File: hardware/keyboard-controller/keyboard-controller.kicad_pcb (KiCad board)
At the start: 2 copper layers, 34 parts, among them J1 Keybed_Connector, J2 Barrel_Jack_Switch, J3 Debug_Pins, J4 CV_OUT, J5 GATE_OUT, U1 L78L09_TO92, U2 LM358, U3 74HC164, U4 74HC164, U5 TL431LP, U6 LM1117-3.3, U7 Pico, U8 MCP4921

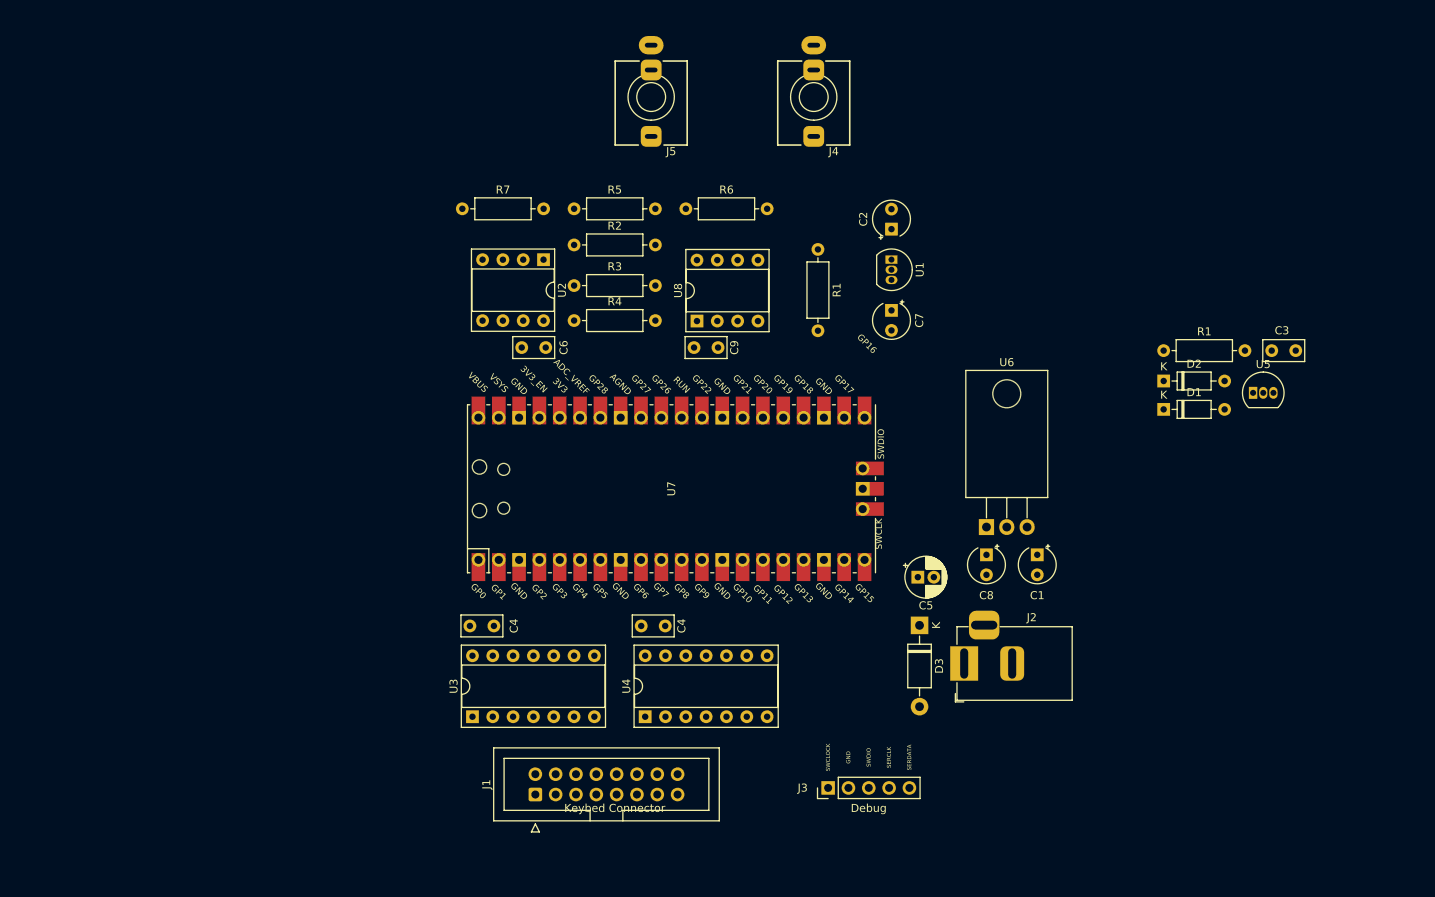
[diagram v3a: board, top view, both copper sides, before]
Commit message: Updated hardware_config and fixed sync_cn
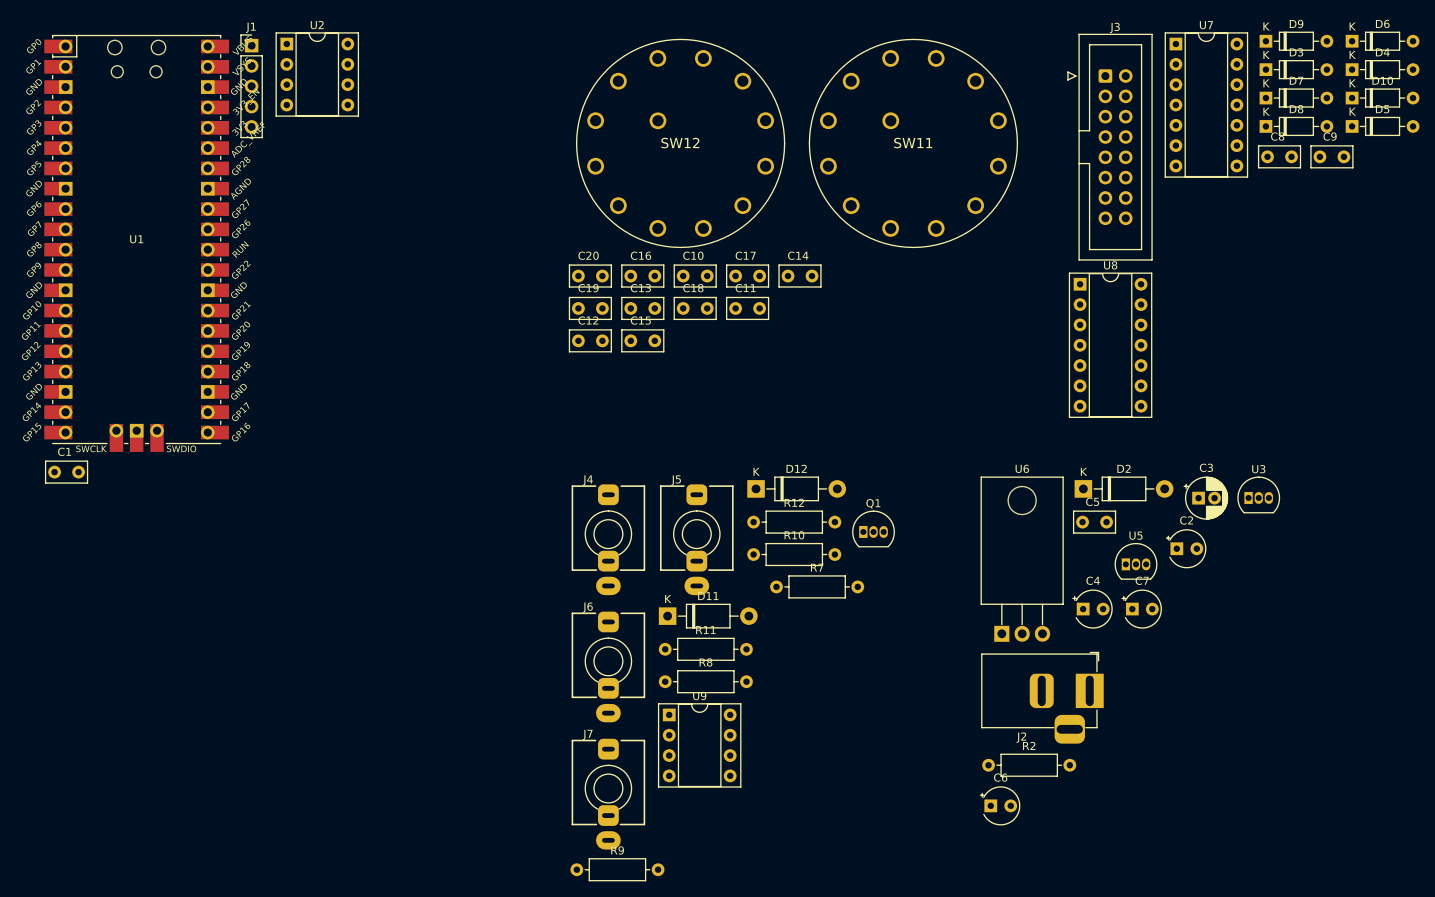
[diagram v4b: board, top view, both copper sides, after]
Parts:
- removed the C4 at (109.9, 114.3)
- removed the C4 at (128.3, 114.3)
- removed D1: 1N4148, Diode_THT:D_DO-35_SOD27_P7.62mm_Horizontal
- removed R1 (x2): 100, Royal_Ohm_Resistors:R_Axial_DIN0207_L6.8mm_D2.5mm_P10.16mm_Horizontal
- removed R3, R4: 10K, Royal_Ohm_Resistors:R_Axial_DIN0207_L6.8mm_D2.5mm_P10.16mm_Horizontal
- removed R5: 22K, Royal_Ohm_Resistors:R_Axial_DIN0207_L6.8mm_D2.5mm_P10.16mm_Horizontal
- removed R6: 1K, Royal_Ohm_Resistors:R_Axial_DIN0207_L6.8mm_D2.5mm_P10.16mm_Horizontal
- removed U4: 74HC164, Package_DIP:DIP-14_W7.62mm_Socket
- added C10: 0.1uF, AEC_Capacitors:C_Disc_D5.0mm_W2.5mm_P3.0mm, F.Cu at (133.6, 70.6)
- added C11: 0.1uF, AEC_Capacitors:C_Disc_D5.0mm_W2.5mm_P3.0mm, F.Cu at (140.1, 74.6)
- added C12: 0.1uF, AEC_Capacitors:C_Disc_D5.0mm_W2.5mm_P3.0mm, F.Cu at (120.5, 78.7)
- added C13: 0.1uF, AEC_Capacitors:C_Disc_D5.0mm_W2.5mm_P3.0mm, F.Cu at (127.0, 74.6)
- added C14: 0.1uF, AEC_Capacitors:C_Disc_D5.0mm_W2.5mm_P3.0mm, F.Cu at (146.7, 70.6)
- added C15: 0.1uF, AEC_Capacitors:C_Disc_D5.0mm_W2.5mm_P3.0mm, F.Cu at (127.0, 78.7)
- added C16: 0.1uF, AEC_Capacitors:C_Disc_D5.0mm_W2.5mm_P3.0mm, F.Cu at (127.0, 70.6)
- added C17: 0.1uF, AEC_Capacitors:C_Disc_D5.0mm_W2.5mm_P3.0mm, F.Cu at (140.1, 70.6)
- added C18: 0.1uF, AEC_Capacitors:C_Disc_D5.0mm_W2.5mm_P3.0mm, F.Cu at (133.6, 74.6)
- added C19: 0.1uF, AEC_Capacitors:C_Disc_D5.0mm_W2.5mm_P3.0mm, F.Cu at (120.5, 74.6)
- added C20: 0.1uF, AEC_Capacitors:C_Disc_D5.0mm_W2.5mm_P3.0mm, F.Cu at (120.5, 70.6)
- added C4: 0.1uF, Capacitor_THT:CP_Radial_Tantal_D4.5mm_P2.50mm, F.Cu at (183.5, 112.2)
- added D10: 1N4148, Diode_THT:D_DO-35_SOD27_P7.62mm_Horizontal, F.Cu at (217.2, 48.3)
- added D11: 1N5818, Diode_THT:D_DO-41_SOD81_P10.16mm_Horizontal, F.Cu at (131.6, 113.1)
- added D12: 1N5818, Diode_THT:D_DO-41_SOD81_P10.16mm_Horizontal, F.Cu at (142.6, 97.2)
- added D4: 1N4148, Diode_THT:D_DO-35_SOD27_P7.62mm_Horizontal, F.Cu at (217.2, 44.8)
- added D5: 1N4148, Diode_THT:D_DO-35_SOD27_P7.62mm_Horizontal, F.Cu at (217.2, 51.9)
- added D6: 1N4148, Diode_THT:D_DO-35_SOD27_P7.62mm_Horizontal, F.Cu at (217.2, 41.2)
- added D7: 1N4148, Diode_THT:D_DO-35_SOD27_P7.62mm_Horizontal, F.Cu at (206.4, 48.3)
- added D8: 1N4148, Diode_THT:D_DO-35_SOD27_P7.62mm_Horizontal, F.Cu at (206.4, 51.9)
- added D9: 1N4148, Diode_THT:D_DO-35_SOD27_P7.62mm_Horizontal, F.Cu at (206.4, 41.2)
- added J6: GATE_OUT, AudioJacks:Jack_3.5mm_QingPu_WQP-PJ398SM_Vertical, F.Cu at (124.2, 118.7)
- added J7: SYNC_OUT, AudioJacks:Jack_3.5mm_QingPu_WQP-PJ398SM_Vertical, F.Cu at (124.2, 134.6)
- added Q1: 2N3904, Package_TO_SOT_THT:TO-92_Inline, F.Cu at (156.1, 102.6)
- added R10: 22K, Royal_Ohm_Resistors:R_Axial_DIN0207_L6.8mm_D2.5mm_P10.16mm_Horizontal, F.Cu at (142.3, 105.4)
- added R11: 1K, Royal_Ohm_Resistors:R_Axial_DIN0207_L6.8mm_D2.5mm_P10.16mm_Horizontal, F.Cu at (131.3, 117.2)
- added R12: 1K, Royal_Ohm_Resistors:R_Axial_DIN0207_L6.8mm_D2.5mm_P10.16mm_Horizontal, F.Cu at (142.3, 101.3)
- added R8: 10K, Royal_Ohm_Resistors:R_Axial_DIN0207_L6.8mm_D2.5mm_P10.16mm_Horizontal, F.Cu at (131.3, 121.3)
- added R9: 10K, Royal_Ohm_Resistors:R_Axial_DIN0207_L6.8mm_D2.5mm_P10.16mm_Horizontal, F.Cu at (120.2, 144.8)
- added SW11: CLK_DIV, SamacSys_Parts:SR2612F011221R0BD8N, F.Cu at (151.7, 51.1)
- added SW12: SUB_MODE, SamacSys_Parts:SR2612F011221R0BD8N, F.Cu at (122.6, 51.1)
- added U9: LM358, Package_DIP:DIP-8_W7.62mm_Socket, F.Cu at (131.8, 125.4)
- C1: value 0.33uF -> 0.1uF; footprint Capacitor_THT:CP_Radial_Tantal_D4.5mm_P2.50mm -> AEC_Capacitors:C_Disc_D5.0mm_W2.5mm_P3.0mm
- C2: value 0.1uF -> 0.33uF
- C3: value 0.1uF -> 47uF; footprint AEC_Capacitors:C_Disc_D5.0mm_W2.5mm_P3.0mm -> Capacitor_THT:CP_Radial_D5.0mm_P2.00mm
- C5: value 47uF -> 0.1uF; footprint Capacitor_THT:CP_Radial_D5.0mm_P2.00mm -> AEC_Capacitors:C_Disc_D5.0mm_W2.5mm_P3.0mm
- C6: value 0.1uF -> 10uF; footprint AEC_Capacitors:C_Disc_D5.0mm_W2.5mm_P3.0mm -> Capacitor_THT:CP_Radial_Tantal_D4.5mm_P2.50mm
- C8: value 100uF -> 0.1uF; footprint Capacitor_THT:CP_Radial_Tantal_D4.5mm_P2.50mm -> AEC_Capacitors:C_Disc_D5.0mm_W2.5mm_P3.0mm
- D2: value 1N4148 -> 1N4001; footprint Diode_THT:D_DO-35_SOD27_P7.62mm_Horizontal -> Diode_THT:D_DO-41_SOD81_P10.16mm_Horizontal
- D3: value 1N5818 -> 1N4148; footprint Diode_THT:D_DO-41_SOD81_P10.16mm_Horizontal -> Diode_THT:D_DO-35_SOD27_P7.62mm_Horizontal
- J1: value Keybed_Connector -> Debug_Pins; footprint Connector_IDC:IDC-Header_2x08_P2.54mm_Vertical -> Connector_PinHeader_2.54mm:PinHeader_1x05_P2.54mm_Vertical
- J3: value Debug_Pins -> Keybed_Connector; footprint Connector_PinHeader_2.54mm:PinHeader_1x05_P2.54mm_Vertical -> Connector_IDC:IDC-Header_2x08_P2.54mm_Vertical
- J4: value CV_OUT -> SYNC_IN
- J5: value GATE_OUT -> CV_OUT
- R2: value 10K -> 100
- R7: value 1K -> 10K
- U1: value L78L09_TO92 -> Pico; footprint Package_TO_SOT_THT:TO-92_Inline -> MCU_RaspberryPi_and_Boards:RPi_Pico_SMD_TH
- U2: value LM358 -> MCP4921
- U3: value 74HC164 -> L78L09_TO92; footprint Package_DIP:DIP-14_W7.62mm_Socket -> Package_TO_SOT_THT:TO-92_Inline
- U7: value Pico -> 74HC164; footprint MCU_RaspberryPi_and_Boards:RPi_Pico_SMD_TH -> Package_DIP:DIP-14_W7.62mm_Socket
- U8: value MCP4921 -> 74HC164; footprint Package_DIP:DIP-8_W7.62mm_Socket -> Package_DIP:DIP-14_W7.62mm_Socket
- moved C1 123.2 mm to (55.0, 95.1), turned to 0 degrees
- moved U3 100.8 mm to (204.2, 98.3), turned to 0 degrees
- moved J1 100.1 mm to (79.6, 41.8), turned to 0 degrees
- moved J3 95.5 mm to (186.3, 45.6), turned to 0 degrees
- moved U1 94.4 mm to (65.2, 66.0), turned to 0 degrees
- moved U7 84.1 mm to (195.1, 41.6), turned to 0 degrees
- moved R2 83.2 mm to (171.7, 131.7)
- moved D3 81.9 mm to (206.4, 44.8), turned to 0 degrees
- moved C6 79.9 mm to (172.0, 136.8), turned to 0 degrees
- moved C9 79.0 mm to (213.2, 55.7), turned to 0 degrees
- moved R7 61.4 mm to (145.2, 109.4)
- moved C8 60.9 mm to (206.6, 55.7), turned to 0 degrees
- moved J4 60.4 mm to (124.2, 102.8), turned to 0 degrees
- moved J5 54.9 mm to (135.2, 102.8), turned to 0 degrees
- moved C2 53.6 mm to (195.2, 104.7), turned to 0 degrees
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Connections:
- C1 pad 1: +12V -> GND
- C1 pad 2: GND -> +3V3
- C2 pad 1: +9V -> +12V
- C3 pad 1: GND -> +12V
- C3 pad 2: +3V3 -> GND
- C5 pad 1: +12V -> +9V
- C6 pad 1: +9V -> +12V
- C7 pad 1: +12V -> +3V3
- C8 pad 1: +3V3 -> GND
- C8 pad 2: GND -> +3V3
- D2 pad 1: Net-(D2-Pad1) -> +12V
- D2 pad 2: MATRIX_R1 -> +9V
- D3 pad 1: +12V -> Net-(D3-Pad1)
- D3 pad 2: Net-(D3-Pad2) -> /MATRIX_R1
- J1 pad 1: MATRIX_C1 -> /SWDCLK
- J1 pad 2: MATRIX_C2 -> GND
- J1 pad 3: MATRIX_C3 -> /SWDIO
- J1 pad 4: MATRIX_C4 -> /SERCLK
- J1 pad 5: MATRIX_C5 -> /SERDATA
- J2 pad 1: Net-(D3-Pad2) -> +12V
- J3 pad 1: SWCLOCK -> /Key Matrix/MATRIX_C1
- J3 pad 2: GND -> /Key Matrix/MATRIX_C2
- J3 pad 3: SWDIO -> /Key Matrix/MATRIX_C3
- J3 pad 4: SERCLK -> /Key Matrix/MATRIX_C4
- J3 pad 5: SERDATA -> /Key Matrix/MATRIX_C5
- J4 pad TN: unconnected-(J4-PadTN) -> Net-(J4-PadTN)
- R2 pad 1: Net-(R2-Pad1) -> VREF
- R2 pad 2: GND -> +3V3
- R7 pad 1: Net-(R4-Pad2) -> Net-(R10-Pad1)
- R7 pad 2: Net-(J5-PadT) -> GND
- U1 pad 1: +9V -> /SERDATA
- U1 pad 2: GND -> /SERCLK
- U1 pad 3: +12V -> GND
- U2 pad 1: Net-(R5-Pad2) -> +3V3
- U2 pad 2: Net-(R2-Pad1) -> /DAC_CS
- U2 pad 3: CV -> /SPI_CLK
- U2 pad 4: GND -> /SPI_DATA
- U2 pad 5: GATE -> GND
- U2 pad 6: Net-(R3-Pad1) -> VREF
- U2 pad 7: Net-(R4-Pad2) -> GND
- U2 pad 8: +9V -> /CV_OUT
- U3 pad 1: SHIFT_DATA -> +9V
- U3 pad 2: +3V3 -> GND
- U3 pad 3: MATRIX_C1 -> +12V
- U7 pad 1: SERDATA -> /MATRIX_DATA
- U7 pad 10: unconnected-(U7-Pad10) -> /Key Matrix/MATRIX_C5
- U7 pad 11: unconnected-(U7-Pad11) -> /Key Matrix/MATRIX_C6
- U7 pad 12: unconnected-(U7-Pad12) -> /Key Matrix/MATRIX_C7
- U7 pad 13: GND -> /Key Matrix/MATRIX_C8
- U7 pad 14: SPI_CLK -> +3V3
- U7 pad 2: SERCLK -> +3V3
- U7 pad 3: GND -> /Key Matrix/MATRIX_C1
- U7 pad 4: unconnected-(U7-Pad4) -> /Key Matrix/MATRIX_C2
- U7 pad 5: unconnected-(U7-Pad5) -> /Key Matrix/MATRIX_C3
- U7 pad 6: unconnected-(U7-Pad6) -> /Key Matrix/MATRIX_C4
- U7 pad 7: GATE -> GND
- U7 pad 8: GND -> /MATRIX_CLK
- U7 pad 9: unconnected-(U7-Pad9) -> +3V3
- U8 pad 1: +3V3 -> /Key Matrix/MATRIX_C8
- U8 pad 2: DAC_CS -> +3V3
- U8 pad 3: SPI_CLK -> /Key Matrix/MATRIX_C9
- U8 pad 4: SPI_DATA -> /MATRIX_JACKS_COL
- U8 pad 5: GND -> unconnected-(U8-Pad5)
- U8 pad 6: VREF -> unconnected-(U8-Pad6)
- U8 pad 8: CV -> /MATRIX_CLK
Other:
- board text removed: "Debug"
- board text removed: "GND"
- board text removed: "Keybed Connector"
- board text removed: "SERCLK"
- board text removed: "SERDATA"
- board text removed: "SWCLOCK"
- board text removed: "SWDIO"

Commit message: Completed schematic rev1. Started placing pcb
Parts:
- added D1: GREEN PWR LED, LED_THT:LED_D5.0mm, F.Cu at (167.9, 184.1)
- added D13: 1N4148, Diode_THT:D_DO-35_SOD27_P7.62mm_Horizontal, F.Cu at (220.3, 204.1)
- added D14: 1N4148, Diode_THT:D_DO-35_SOD27_P7.62mm_Horizontal, F.Cu at (234.1, 204.9)
- added D15: 1N5818, Diode_THT:D_DO-41_SOD81_P10.16mm_Horizontal, F.Cu at (291.5, 82.2)
- added D16: 1N5818, Diode_THT:D_DO-41_SOD81_P10.16mm_Horizontal, F.Cu at (281.1, 76.8)
- added R1: 470, Royal_Ohm_Resistors:R_Axial_DIN0207_L6.8mm_D2.5mm_P10.16mm_Horizontal, F.Cu at (162.8, 176.6)
- added R13: 10K, Royal_Ohm_Resistors:R_Axial_DIN0207_L6.8mm_D2.5mm_P10.16mm_Horizontal, F.Cu at (246.6, 78.2)
- added R14: 10K, Royal_Ohm_Resistors:R_Axial_DIN0207_L6.8mm_D2.5mm_P10.16mm_Horizontal, F.Cu at (240.7, 78.3)
- added R15: 22K, Royal_Ohm_Resistors:R_Axial_DIN0207_L6.8mm_D2.5mm_P10.16mm_Horizontal, F.Cu at (212.2, 78.7)
- added R16: 1K, Royal_Ohm_Resistors:R_Axial_DIN0207_L6.8mm_D2.5mm_P10.16mm_Horizontal, F.Cu at (223.7, 58.3)
- added R17: 1K, Royal_Ohm_Resistors:R_Axial_DIN0207_L6.8mm_D2.5mm_P10.16mm_Horizontal, F.Cu at (240.5, 58.1)
- added R18: 1K, Royal_Ohm_Resistors:R_Axial_DIN0207_L6.8mm_D2.5mm_P10.16mm_Horizontal, F.Cu at (287.4, 64.3)
- added R19: 2.2K, Royal_Ohm_Resistors:R_Axial_DIN0207_L6.8mm_D2.5mm_P10.16mm_Horizontal, F.Cu at (81.7, 93.8)
- added R20: 2.2K, Royal_Ohm_Resistors:R_Axial_DIN0207_L6.8mm_D2.5mm_P10.16mm_Horizontal, F.Cu at (85.7, 83.7)
- added R21: 2.2K, Royal_Ohm_Resistors:R_Axial_DIN0207_L6.8mm_D2.5mm_P10.16mm_Horizontal, F.Cu at (89.7, 97.1)
- added R22: 2.2K, Royal_Ohm_Resistors:R_Axial_DIN0207_L6.8mm_D2.5mm_P10.16mm_Horizontal, F.Cu at (115.6, 97.1)
- added R23: 2.2K, Royal_Ohm_Resistors:R_Axial_DIN0207_L6.8mm_D2.5mm_P10.16mm_Horizontal, F.Cu at (119.3, 83.6)
- added R24: 2.2K, Royal_Ohm_Resistors:R_Axial_DIN0207_L6.8mm_D2.5mm_P10.16mm_Horizontal, F.Cu at (124.4, 93.4)
- added R25: 2.2K, Royal_Ohm_Resistors:R_Axial_DIN0207_L6.8mm_D2.5mm_P10.16mm_Horizontal, F.Cu at (118.9, 79.5)
- added R26: 2.2K, Royal_Ohm_Resistors:R_Axial_DIN0207_L6.8mm_D2.5mm_P10.16mm_Horizontal, F.Cu at (124.3, 79.4)
- added R27: 2.2K, Royal_Ohm_Resistors:R_Axial_DIN0207_L6.8mm_D2.5mm_P10.16mm_Horizontal, F.Cu at (113.6, 63.5)
- added R28: 2.2K, Royal_Ohm_Resistors:R_Axial_DIN0207_L6.8mm_D2.5mm_P10.16mm_Horizontal, F.Cu at (99.9, 63.7)
- added R29: 2.2K, Royal_Ohm_Resistors:R_Axial_DIN0207_L6.8mm_D2.5mm_P10.16mm_Horizontal, F.Cu at (85.7, 78.0)
- added R3: 470, Royal_Ohm_Resistors:R_Axial_DIN0207_L6.8mm_D2.5mm_P10.16mm_Horizontal, F.Cu at (190.1, 177.6)
- added R30: 2.2K, Royal_Ohm_Resistors:R_Axial_DIN0207_L6.8mm_D2.5mm_P10.16mm_Horizontal, F.Cu at (80.1, 78.0)
- added R31: 2.2K, Royal_Ohm_Resistors:R_Axial_DIN0207_L6.8mm_D2.5mm_P10.16mm_Horizontal, F.Cu at (78.6, 151.3)
- added R32: 2.2K, Royal_Ohm_Resistors:R_Axial_DIN0207_L6.8mm_D2.5mm_P10.16mm_Horizontal, F.Cu at (84.3, 151.3)
- added R33: 2.2K, Royal_Ohm_Resistors:R_Axial_DIN0207_L6.8mm_D2.5mm_P10.16mm_Horizontal, F.Cu at (89.7, 155.9)
- added R34: 2.2K, Royal_Ohm_Resistors:R_Axial_DIN0207_L6.8mm_D2.5mm_P10.16mm_Horizontal, F.Cu at (105.0, 156.0)
- added R35: 2.2K, Royal_Ohm_Resistors:R_Axial_DIN0207_L6.8mm_D2.5mm_P10.16mm_Horizontal, F.Cu at (119.3, 152.2)
- added R36: 2.2K, Royal_Ohm_Resistors:R_Axial_DIN0207_L6.8mm_D2.5mm_P10.16mm_Horizontal, F.Cu at (124.0, 152.2)
- added R37: 2.2K, Royal_Ohm_Resistors:R_Axial_DIN0207_L6.8mm_D2.5mm_P10.16mm_Horizontal, F.Cu at (119.7, 136.8)
- added R38: 2.2K, Royal_Ohm_Resistors:R_Axial_DIN0207_L6.8mm_D2.5mm_P10.16mm_Horizontal, F.Cu at (124.8, 136.9)
- added R39: 2.2K, Royal_Ohm_Resistors:R_Axial_DIN0207_L6.8mm_D2.5mm_P10.16mm_Horizontal, F.Cu at (115.2, 120.8)
- added R4: 470, Royal_Ohm_Resistors:R_Axial_DIN0207_L6.8mm_D2.5mm_P10.16mm_Horizontal, F.Cu at (206.9, 177.4)
- added R40: 2.2K, Royal_Ohm_Resistors:R_Axial_DIN0207_L6.8mm_D2.5mm_P10.16mm_Horizontal, F.Cu at (99.7, 121.0)
- added R41: 2.2K, Royal_Ohm_Resistors:R_Axial_DIN0207_L6.8mm_D2.5mm_P10.16mm_Horizontal, F.Cu at (84.5, 126.0)
- added R42: 2.2K, Royal_Ohm_Resistors:R_Axial_DIN0207_L6.8mm_D2.5mm_P10.16mm_Horizontal, F.Cu at (79.7, 136.1)
- added R5: 470, Royal_Ohm_Resistors:R_Axial_DIN0207_L6.8mm_D2.5mm_P10.16mm_Horizontal, F.Cu at (225.7, 177.9)
- added R6: 100, Royal_Ohm_Resistors:R_Axial_DIN0207_L6.8mm_D2.5mm_P10.16mm_Horizontal, F.Cu at (246.7, 90.3)
- added RV1: CLK_SPEED, Alpha_Potentiometers:Potentiometer_Alpha_RV09AF-40-20K-B1K_Single_Vertical, F.Cu at (151.3, 74.0)
- added RV2: PORTAMENTO, Alpha_Potentiometers:Potentiometer_Alpha_RV09AF-40-20K-B1K_Single_Vertical, F.Cu at (150.8, 105.3)
- added RV3: GATE_TIME, Alpha_Potentiometers:Potentiometer_Alpha_RV09AF-40-20K-B1K_Single_Vertical, F.Cu at (151.5, 144.1)
- added SW1: RESET, Button_Switch_THT:SW_PUSH_6mm, F.Cu at (242.1, 152.6)
- added SW10: FUNCTION, Button_Switch_THT:SW_PUSH_6mm, F.Cu at (234.7, 192.2)
- added SW2: MODE_SEL, Wealth_Metal_Switches:Slide_Switch_SPDT_SS12F44G5, F.Cu at (194.0, 135.5)
- added SW3: OCTAVE_UP, Button_Switch_THT:SW_PUSH_6mm, F.Cu at (136.4, 192.0)
- added SW4: OCTAVE_DOWN, Button_Switch_THT:SW_PUSH_6mm, F.Cu at (151.6, 192.1)
- added SW5: PLAY_PAUSE, Button_Switch_THT:SW_PUSH_6mm, F.Cu at (165.2, 192.1)
- added SW6: RECORD, Button_Switch_THT:SW_PUSH_6mm, F.Cu at (179.1, 192.5)
- added SW7: STOP, Button_Switch_THT:SW_PUSH_6mm, F.Cu at (192.8, 192.7)
- added SW8: REST, Button_Switch_THT:SW_PUSH_6mm, F.Cu at (205.9, 192.7)
- added SW9: HOLD, Button_Switch_THT:SW_PUSH_6mm, F.Cu at (220.7, 193.1)
- added U4: TL431LP, Package_TO_SOT_THT:TO-92_Inline, F.Cu at (248.0, 85.2)
- C2: value 0.33uF -> 0.1uF; footprint Capacitor_THT:CP_Radial_Tantal_D4.5mm_P2.50mm -> AEC_Capacitors:C_Disc_D5.0mm_W2.5mm_P3.0mm
- C3: value 47uF -> 0.33uF; footprint Capacitor_THT:CP_Radial_D5.0mm_P2.00mm -> Capacitor_THT:CP_Radial_Tantal_D4.5mm_P2.50mm
- C5: value 0.1uF -> 10uF; footprint AEC_Capacitors:C_Disc_D5.0mm_W2.5mm_P3.0mm -> Capacitor_THT:CP_Radial_Tantal_D4.5mm_P2.50mm
- C7: value 10uF -> 0.1uF; footprint Capacitor_THT:CP_Radial_Tantal_D4.5mm_P2.50mm -> AEC_Capacitors:C_Disc_D5.0mm_W2.5mm_P3.0mm
- D11, D12: value 1N5818 -> 1N4148; footprint Diode_THT:D_DO-41_SOD81_P10.16mm_Horizontal -> Diode_THT:D_DO-35_SOD27_P7.62mm_Horizontal
- D2: value 1N4001 -> LED1; footprint Diode_THT:D_DO-41_SOD81_P10.16mm_Horizontal -> LED_THT:LED_D5.0mm
- D3: value 1N4148 -> LED2; footprint Diode_THT:D_DO-35_SOD27_P7.62mm_Horizontal -> LED_THT:LED_D5.0mm
- D4: value 1N4148 -> LED3; footprint Diode_THT:D_DO-35_SOD27_P7.62mm_Horizontal -> LED_THT:LED_D5.0mm
- D5: value 1N4148 -> LED4; footprint Diode_THT:D_DO-35_SOD27_P7.62mm_Horizontal -> LED_THT:LED_D5.0mm
- D6: value 1N4148 -> 1N4001; footprint Diode_THT:D_DO-35_SOD27_P7.62mm_Horizontal -> Diode_THT:D_DO-41_SOD81_P10.16mm_Horizontal
- J3: value Keybed_Connector -> Keybed Connector
- R10: value 22K -> 1M
- R11: value 1K -> 1k
- R12: value 1K -> 10K
- R2: value 100 -> 470
- R7: value 10K -> 1K
- R8: value 10K -> 100K
- R9: value 10K -> 1M
- U5: value TL431LP -> LM1117-3.3; footprint Package_TO_SOT_THT:TO-92_Inline -> Package_TO_SOT_THT:TO-220-3_Horizontal_TabDown
- U6: value LM1117-3.3 -> 74HC164; footprint Package_TO_SOT_THT:TO-220-3_Horizontal_TabDown -> Package_DIP:DIP-14_W7.62mm_Socket
- U8: value 74HC164 -> LM358; footprint Package_DIP:DIP-14_W7.62mm_Socket -> Package_DIP:DIP-8_W7.62mm_Socket
- U9: value LM358 -> CD4051B; footprint Package_DIP:DIP-8_W7.62mm_Socket -> Package_DIP:DIP-16_W7.62mm_Socket
- moved C1 220.3 mm to (270.5, 140.6)
- moved D6 198.3 mm to (85.1, 189.1)
- moved U1 188.8 mm to (245.5, 122.2), turned to -90 degrees
- moved J3 188.4 mm to (222.5, 230.5), turned to 90 degrees
- moved J7 187.1 mm to (292.0, 51.9)
- moved U7 186.2 mm to (259.8, 216.2)
- moved D7 171.3 mm to (135.4, 204.3)
- moved R9 170.8 mm to (273.4, 69.2), turned to 180 degrees
- moved D9 168.2 mm to (163.7, 203.9)
- moved C8 165.1 mm to (257.7, 212.7)
- moved D8 162.3 mm to (150.5, 204.2)
- moved D10 159.9 mm to (178.1, 203.4)
- moved J4 153.1 mm to (268.9, 52.9)
- moved U3 153.0 mm to (85.2, 194.5)
- moved U5 152.0 mm to (74.9, 207.2)
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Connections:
- C2 pad 1: +12V -> GND
- C2 pad 2: GND -> +3V3
- C5 pad 1: +9V -> +12V
- C6 pad 1: +12V -> +3V3
- C7 pad 1: +3V3 -> GND
- C7 pad 2: GND -> +3V3
- C9 pad 1: GND -> +9V
- C9 pad 2: +3V3 -> GND
- D10 pad 2: /MATRIX_R3 -> /MATRIX_R4
- D11 pad 1: +3V3 -> Net-(D11-Pad1)
- D11 pad 2: /SYNC_CN -> /MATRIX_R5
- D12 pad 1: /SYNC_CN -> Net-(D12-Pad1)
- D12 pad 2: GND -> /MATRIX_R1
- D2 pad 1: +12V -> Net-(D2-Pad1)
- D2 pad 2: +9V -> /LED1
- D3 pad 2: /MATRIX_R1 -> /LED2
- D4 pad 2: /MATRIX_R2 -> /LED3
- D5 pad 2: /MATRIX_R3 -> /LED4
- D6 pad 1: Net-(D6-Pad1) -> +12V
- D6 pad 2: /MATRIX_R4 -> +9V
- D7 pad 2: /MATRIX_R5 -> /MATRIX_R1
- D8 pad 2: /MATRIX_R1 -> /MATRIX_R2
- D9 pad 2: /MATRIX_R2 -> /MATRIX_R3
- J3 pad 16: (no net) -> unconnected-(J3-Pad16)
- R10 pad 1: Net-(R10-Pad1) -> /SYNC_CN
- R10 pad 2: Net-(R10-Pad2) -> +3V3
- R11 pad 1: Net-(R10-Pad2) -> +3V3
- R11 pad 2: Net-(J5-PadT) -> /SYNC_IN
- R12 pad 2: Net-(J6-PadT) -> GND
- R2 pad 1: VREF -> Net-(D2-Pad1)
- R2 pad 2: +3V3 -> GND
- R7 pad 1: Net-(R10-Pad1) -> Net-(J4-PadTN)
- R7 pad 2: GND -> /SYNC_CN
- R8 pad 1: Net-(R8-Pad1) -> Net-(J4-PadT)
- R8 pad 2: GND -> Net-(Q1-Pad2)
- R9 pad 1: Net-(R8-Pad1) -> Net-(Q1-Pad2)
- R9 pad 2: Net-(R12-Pad1) -> GND
- U1 pad 12: /MODE_SEL -> /DAC_CS
- U1 pad 16: unconnected-(U1-Pad16) -> /LED4
- U1 pad 17: /DAC_CS -> /LED3
- U1 pad 19: /MATRIX_CLK -> /LED2
- U1 pad 20: /MATRIX_DATA -> /LED1
- U1 pad 32: unconnected-(U1-Pad32) -> /MATRIX_CLK
- U1 pad 34: unconnected-(U1-Pad34) -> /MATRIX_DATA
- U5 pad 1: VREF -> GND
- U5 pad 2: GND -> +3V3
- U5 pad 3: VREF -> +12V
- U6 pad 1: GND -> /MATRIX_DATA
- U6 pad 3: +12V -> /Key Matrix/MATRIX_C1
- U7 pad 1: /MATRIX_DATA -> /Key Matrix/MATRIX_C8
- U7 pad 10: /Key Matrix/MATRIX_C5 -> unconnected-(U7-Pad10)
- U7 pad 11: /Key Matrix/MATRIX_C6 -> unconnected-(U7-Pad11)
- U7 pad 12: /Key Matrix/MATRIX_C7 -> unconnected-(U7-Pad12)
- U7 pad 13: /Key Matrix/MATRIX_C8 -> unconnected-(U7-Pad13)
- U7 pad 3: /Key Matrix/MATRIX_C1 -> /Key Matrix/MATRIX_C9
- U7 pad 4: /Key Matrix/MATRIX_C2 -> /Key Matrix/MATRIX_C10
- U7 pad 5: /Key Matrix/MATRIX_C3 -> unconnected-(U7-Pad5)
- U7 pad 6: /Key Matrix/MATRIX_C4 -> unconnected-(U7-Pad6)
- U8 pad 1: /Key Matrix/MATRIX_C8 -> Net-(R15-Pad2)
- U8 pad 2: +3V3 -> Net-(R12-Pad1)
- U8 pad 3: /Key Matrix/MATRIX_C9 -> /CV_OUT
- U8 pad 4: /MATRIX_JACKS_COL -> GND
- U8 pad 5: unconnected-(U8-Pad5) -> /GATE_OUT
- U8 pad 6: unconnected-(U8-Pad6) -> Net-(R13-Pad1)
- U8 pad 7: GND -> Net-(R14-Pad2)
- U8 pad 8: /MATRIX_CLK -> +9V
- U9 pad 1: Net-(R10-Pad2) -> /analog_input/SUB_MODE
- U9 pad 2: Net-(R10-Pad1) -> GND
- U9 pad 3: /CV_OUT -> /ANALOG_IN
- U9 pad 4: (no net) -> GND
- U9 pad 5: /GATE_OUT -> GND
- U9 pad 6: Net-(R8-Pad1) -> GND
- U9 pad 7: Net-(R12-Pad1) -> GND
- U9 pad 8: (no net) -> GND
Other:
- board outline added: 249.7 x 210 mm
- copper layers 2 -> 4
